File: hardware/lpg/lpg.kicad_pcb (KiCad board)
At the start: 2 copper layers, 40 x 100 mm, 66 parts, among them J1 AudioJack2_SwitchT, J2 AudioJack2_SwitchT, J3 AudioJack2_SwitchT, J4 AudioJack2_SwitchT, J5 Conn_02x05_Odd_Even, Q1 BC547, Q2 BC547, SW1 SW_3PDT_x3, SW2 SW_DPDT_x2, U1 TL074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

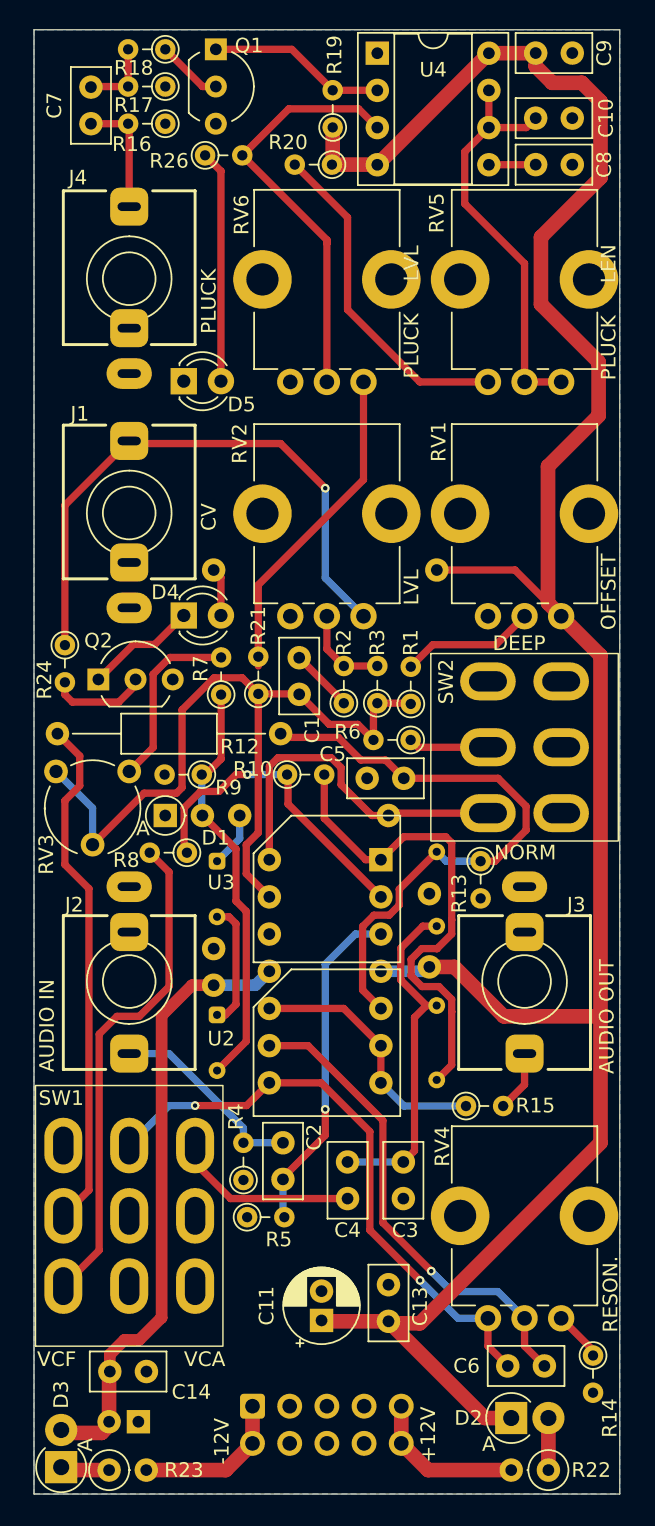
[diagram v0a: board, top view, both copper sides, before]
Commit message: replaced switches with 4P3T slider and SPDT M5 sub-mini toggle
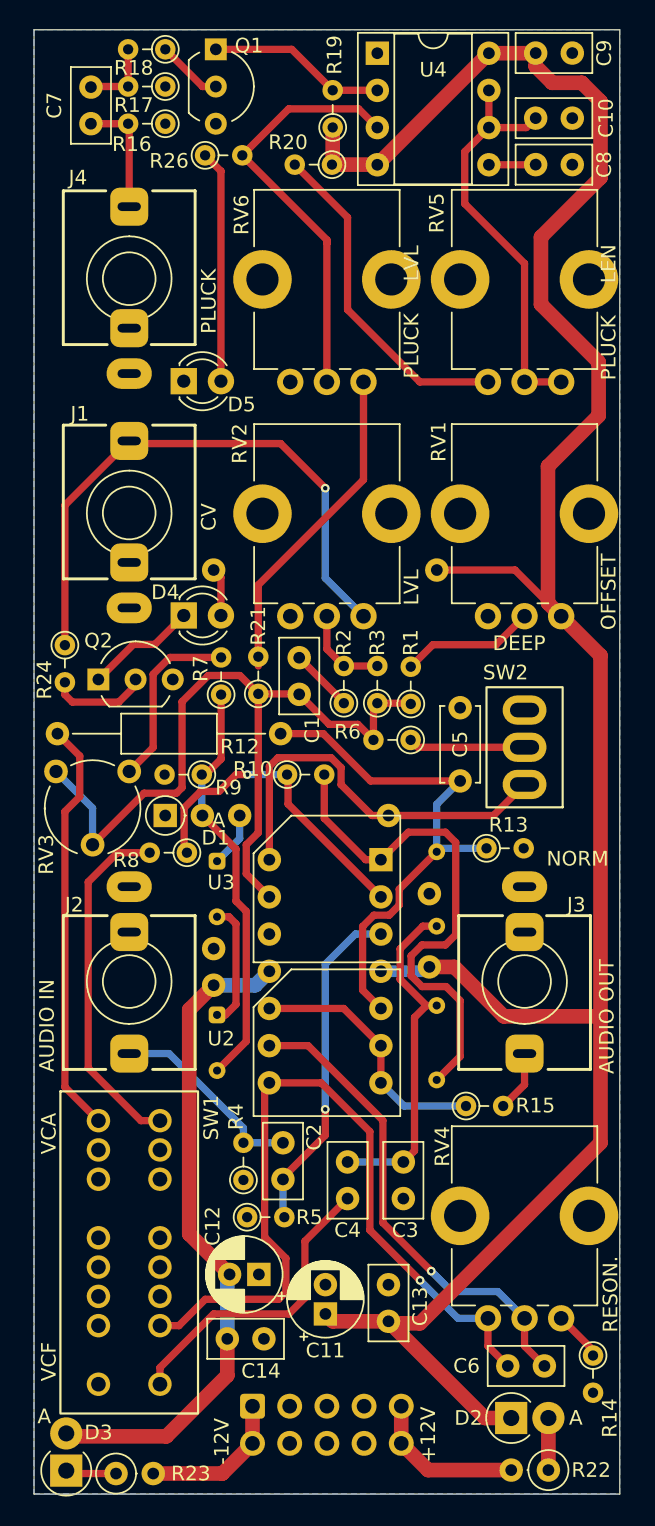
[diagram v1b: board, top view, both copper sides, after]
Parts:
- C12: moved to F.Cu
- C5: footprint Capacitor_THT:C_Disc_D5.0mm_W2.5mm_P2.50mm -> Capacitor_THT:C_Disc_D5.0mm_W2.5mm_P5.00mm
- SW1: value SW_3PDT_x3 -> SW_4P3T_x4; footprint Switches:SW_3PDT_18mm_x_13mm_P4.50mm -> Switches:SW_4P3T_SS-43D01_NoFrame
- SW2: value SW_DPDT_x2 -> SW_SPDT; footprint Switches:SW_DPDT_13mm_x_13mm_P5.00mm -> Switches:SW_Dailywell_SPDT_2MS1T1B1M1
- moved C12 13.0 mm to (115.4, 105.0)
- moved C14 8.33 mm to (113.2, 109.4)
- moved C5 7.97 mm to (129.1, 66.3), turned to -90 degrees
- moved SW1 2.50 mm to (106.5, 103.5), turned to 0 degrees
- moved R13 0.97 mm to (130.9, 75.9), turned to 0 degrees
- moved R23 0.53 mm to (105.6, 118.6)
- moved C11 0.52 mm to (119.9, 107.7)
- moved D3 0.42 mm to (102.2, 118.4)
- turned SW2 to 180 degrees
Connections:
- C4 pad 1: Net-(SW1C-C) -> Net-(C4-Pad1)
- C6 pad 2: Net-(SW1C-B) -> Net-(C6-Pad2)
- R12 pad 2: Net-(SW1B-A) -> Net-(R12-Pad2)
- R8 pad 2: Net-(SW1A-A) -> Net-(R8-Pad2)
- RV4 pad 3: Net-(SW1C-B) -> Net-(C6-Pad2)
- SW1 pad 1: Net-(SW1A-A) -> Net-(R12-Pad2)
- SW1 pad 2: GND -> unconnected-(SW1-Pad2)
- SW1 pad 3: unconnected-(SW1A-C-Pad3) -> GND
- SW1 pad 4: Net-(SW1B-A) -> unconnected-(SW1-Pad4)
- SW1 pad 5: GND -> unconnected-(SW1-Pad5)
- SW1 pad 8: Net-(SW1C-B) -> unconnected-(SW1-Pad8)
- SW1 pad 9: Net-(SW1C-C) -> Net-(R8-Pad2)
- U1 pad 8: Net-(SW1C-B) -> Net-(C6-Pad2)
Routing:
- net Net-(C6-Pad2): track 0.00 -> 54.1 mm, vias 0 -> 1
- net Net-(SW1C-B): track 40.8 -> 0.00 mm, vias 2 -> 0
- net Net-(SW1B-A): track 35.4 -> 0.00 mm
- net Net-(SW1A-A): track 34.0 -> 0.00 mm
- net Net-(R12-Pad2): track 0.00 -> 28.4 mm
- net Net-(R8-Pad2): track 0.00 -> 24.1 mm
- net Net-(C4-Pad1): track 0.00 -> 21.0 mm
- net Net-(SW1C-C): track 12.6 -> 0.00 mm
- net Net-(U1B-+): track 41.6 -> 36.5 mm
- net -12V: track 42.2 -> 45.5 mm
- net Net-(SW2-C): track 24.2 -> 27.2 mm
- net Net-(SW2-B): track 5.49 -> 7.99 mm
- net /vif: track 33.9 -> 35.6 mm
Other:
- board text added: "idyllm CC BY-SA 4.0 v1.1.20250509"
- board text removed: "idyllm CC BY-SA 4.0 v1.0.20240930"
